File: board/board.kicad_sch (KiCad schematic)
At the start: 0 parts

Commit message: The microcontroller
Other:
- added sheet Micrcontroller (micrcontroller.kicad_sch)
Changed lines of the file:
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@@
+		)
+	)
+	(sheet
+		(at 77.47 15.24)
+		(size 48.26 29.21)
+		(exclude_from_sim no)
+		(in_bom yes)
+		(on_board yes)
+		(dnp no)
+		(fields_autoplaced yes)
+		(stroke
+			(width 0.1524)
+			(type solid)
+		)
+		(fill
+			(color 0 0 0 0.0000)
+		)
+		(property "Sheetname" "Micrcontroller"
+			(at 77.47 14.5284 0)
+			(effects
+				(font
+					(size 1.27 1.27)
+				)
+				(justify left bottom)
+			)
+		)
+		(property "Sheetfile" "micrcontroller.kicad_sch"
+			(at 77.47 45.0346 0)
+			(effects
+				(font
+					(size 1.27 1.27)
+				)
+				(justify left top)
+			)
+		)
+		(instances
+			(project "board"
+				(path "/380d0889-29f1-4d98-b1bb-ce6ede3c8d67"
+					(page "3")
+				)
+			)
 		)
 	)

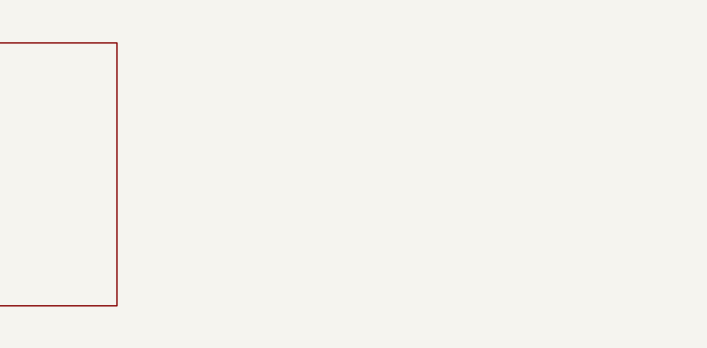
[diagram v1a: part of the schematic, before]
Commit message: Display Schematic
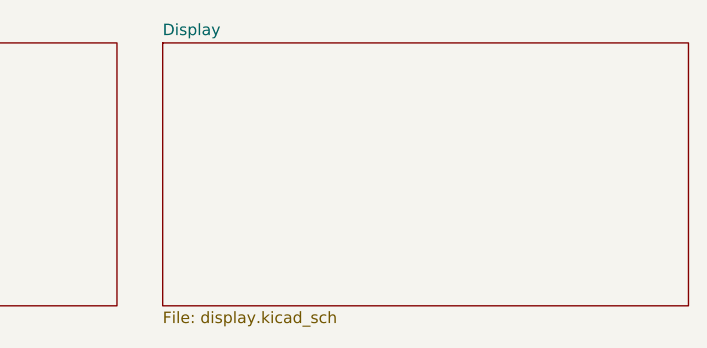
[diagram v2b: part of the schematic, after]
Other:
- added sheet Display (display.kicad_sch)
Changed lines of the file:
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@@
+	)
+	(sheet
+		(at 130.81 15.24)
+		(size 58.42 29.21)
+		(exclude_from_sim no)
+		(in_bom yes)
+		(on_board yes)
+		(dnp no)
+		(fields_autoplaced yes)
+		(stroke
+			(width 0.1524)
+			(type solid)
+		)
+		(fill
+			(color 0 0 0 0.0000)
+		)
+		(property "Sheetname" "Display"
+			(at 130.81 14.5284 0)
+			(effects
+				(font
+					(size 1.27 1.27)
+				)
+				(justify left bottom)
+			)
+		)
+		(property "Sheetfile" "display.kicad_sch"
+			(at 130.81 45.0346 0)
+			(effects
+				(font
+					(size 1.27 1.27)
+				)
+				(justify left top)
+			)
+		)
+		(instances
+			(project "board"
+				(path "/380d0889-29f1-4d98-b1bb-ce6ede3c8d67"
+					(page "4")
+				)
+			)
+		)
 	)
 	(sheet

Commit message: Finishing touches on the PCB
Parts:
- added H1, H2, H3, H4, H5, H6: MountingHole, MountingHole:MountingHole_2.2mm_M2, symbol Mechanical:MountingHole
